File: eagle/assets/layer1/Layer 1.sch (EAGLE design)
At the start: 248 parts, among them M1C1 33nF, M1C2 680uF, M1C3 1.0uF, M1D1 RED, M1D2 BLUE, M1J1 XT30PB-F, M1Q1 AOD482, M1R1 1k, M1R10 1k, M1R11 10k, M1R12 4.7k, M1R2 1k, M1R3 3.3k, M1R4 3.3k, M1R5 1k, M1R6 1k, M1R7 1k, M1R8 10k, M1R9 10k, M2C1 33nF, M2C2 680uF, M2C3 1.0uF, M2D1 RED, M2D2 BLUE, M2J1 XT30PB-F, M2Q1 AOD482, M2R1 1k, M2R10 1k, M2R11 10k, M2R12 4.7k, M2R2 1k, M2R3 3.3k, M2R4 3.3k, M2R5 1k, M2R6 1k, M2R7 1k, M2R8 10k, M2R9 10k, M3C1 33nF, M3C2 680uF, M3C3 1.0uF, M3D1 RED, M3D2 BLUE, M3J1 XT30PB-F, M3Q1 AOD482, M3R1 1k, M3R10 1k, M3R11 10k, M3R12 4.7k, M3R2 1k, M3R3 3.3k, M3R4 3.3k, M3R5 1k, M3R6 1k, M3R7 1k, M3R8 10k, M3R9 10k, M4C1 33nF, M4C2 680uF, M4C3 1.0uF, M4D1 RED, M4D2 BLUE, M4J1 XT30PB-F, M4Q1 AOD482, M4R1 1k, M4R10 1k, M4R11 10k, M4R12 4.7k, M4R2 1k, M4R3 3.3k, M4R4 3.3k, M4R5 1k, M4R6 1k, M4R7 1k, M4R8 10k, M4R9 10k, Q1 LIGHT_SENSORALS, Q10 LIGHT_SENSORALS, Q11 LIGHT_SENSORALS, Q12 LIGHT_SENSORALS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

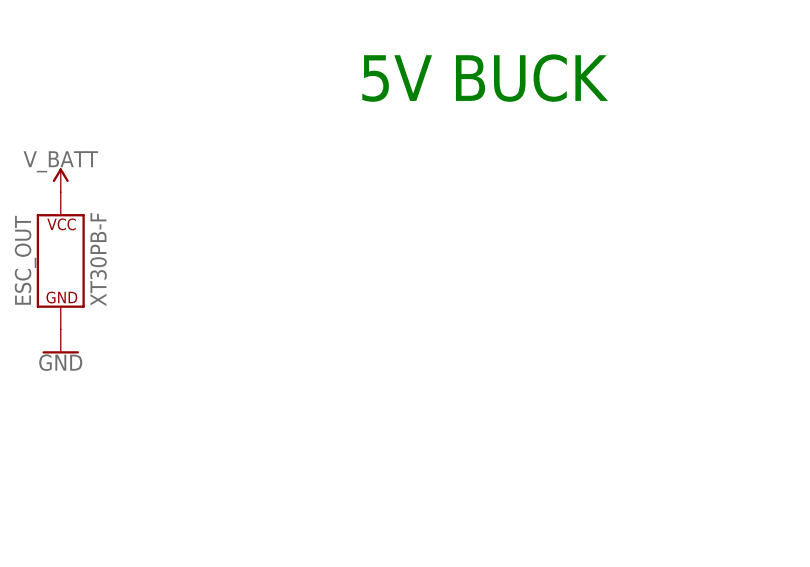
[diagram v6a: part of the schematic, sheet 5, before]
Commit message: Added GND Connector
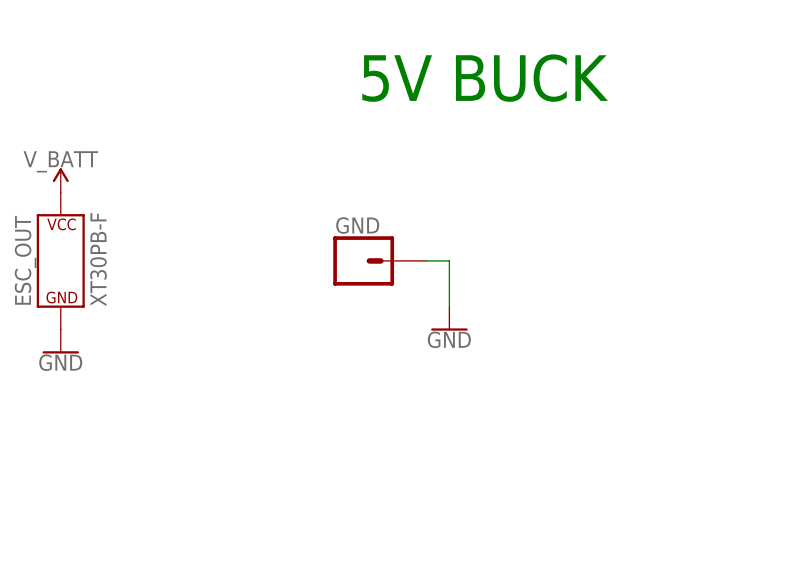
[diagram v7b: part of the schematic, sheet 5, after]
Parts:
- added GND: (no value), SparkFun-Connectors:CONN_01
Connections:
- net GND: now also GND.1
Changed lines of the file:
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@@
 <part name="R10" library="JH" library_urn="urn:adsk.eagle:library:6027132" deviceset="RESISTOR" device="0603" package3d_urn="urn:adsk.eagle:package:15441228/3" value="10k"/>
 <part name="GND40" library="SparkFun-PowerSymbols" deviceset="GND" device=""/>
+<part name="GND" library="SparkFun-Connectors" library_urn="urn:adsk.eagle:library:513" deviceset="CONN_01" device="" package3d_urn="urn:adsk.eagle:package:38028/1"/>
+<part name="GND41" library="SparkFun-PowerSymbols" deviceset="GND" device=""/>
 </parts>
 <sheets>
@@
 <attribute name="NAME" x="10.16" y="58.928" size="1.778" layer="95" font="vector"/>
 </instance>
+<instance part="GND" gate="G$1" x="43.18" y="20.32" smashed="yes">
+<attribute name="VALUE" x="40.64" y="15.494" size="1.778" layer="96" font="vector"/>
+<attribute name="NAME" x="40.64" y="23.368" size="1.778" layer="95" font="vector"/>
+</instance>
+<instance part="GND41" gate="1" x="53.34" y="12.7" smashed="yes">
+<attribute name="VALUE" x="53.34" y="12.446" size="1.778" layer="96" align="top-center"/>
+</instance>
 </instances>
 <busses>
@@
 <pinref part="GND39" gate="1" pin="GND"/>
 </segment>
+<segment>
+<pinref part="GND" gate="G$1" pin="1"/>
+<pinref part="GND41" gate="1" pin="GND"/>
+<wire x1="50.8" y1="20.32" x2="53.34" y2="20.32" width="0.1524" layer="91"/>
+<wire x1="53.34" y1="20.32" x2="53.34" y2="15.24" width="0.1524" layer="91"/>
+</segment>
 </net>

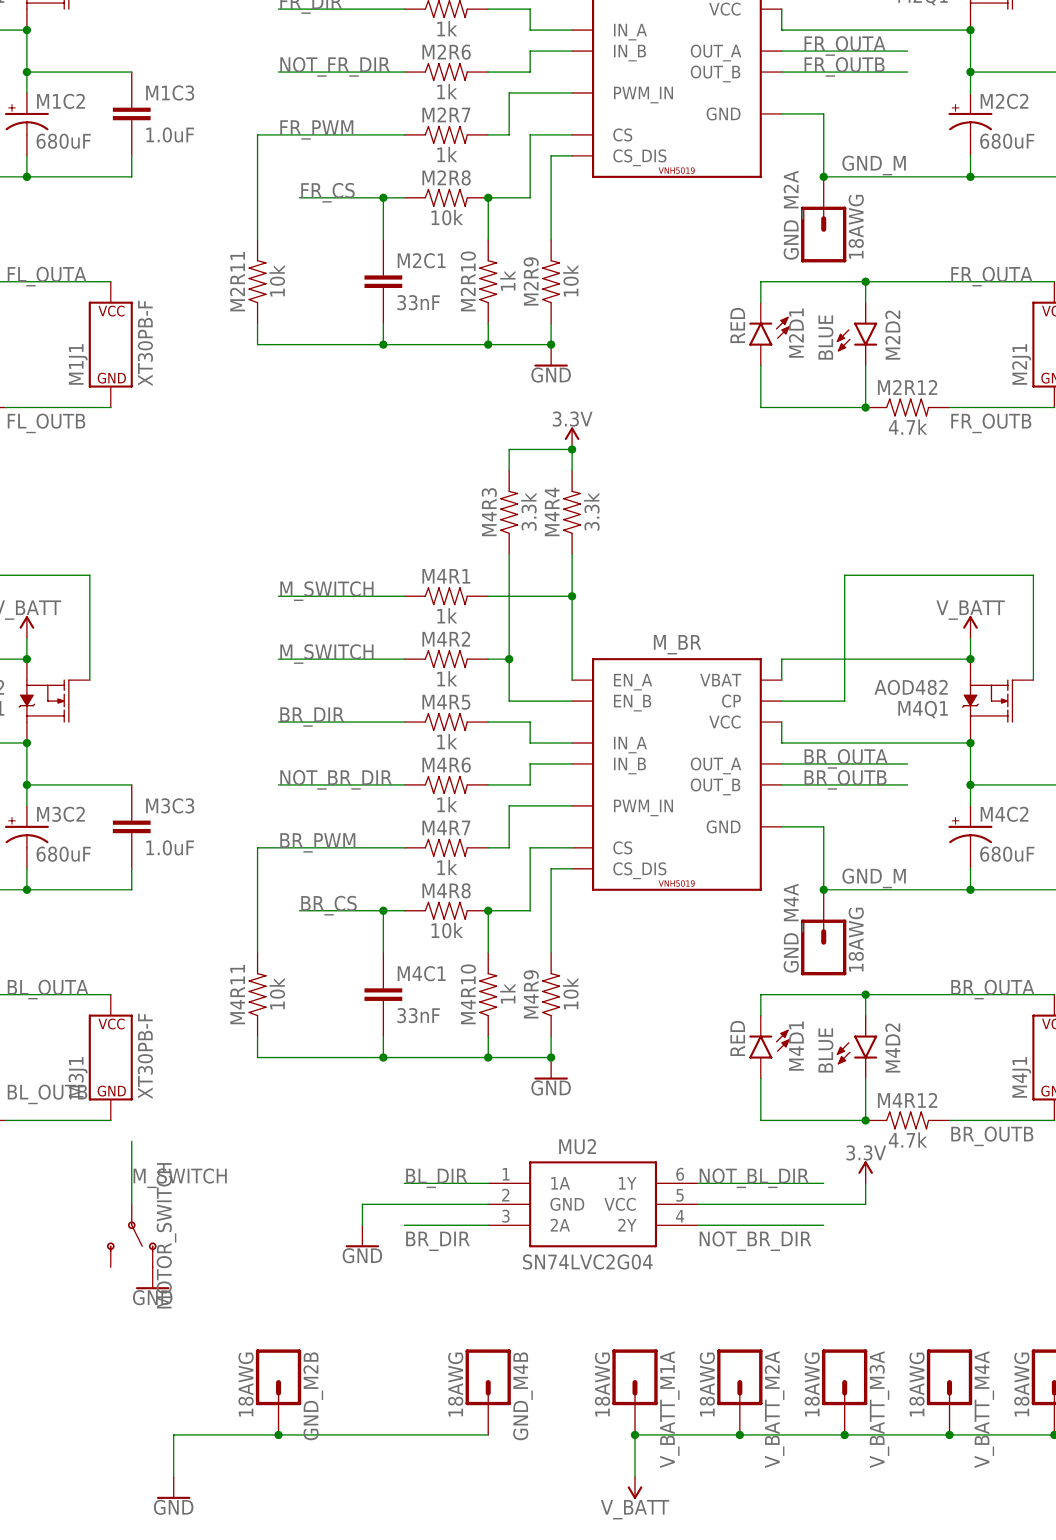
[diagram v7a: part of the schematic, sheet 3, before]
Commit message: Removed Motor Ground and Added battery mount holes
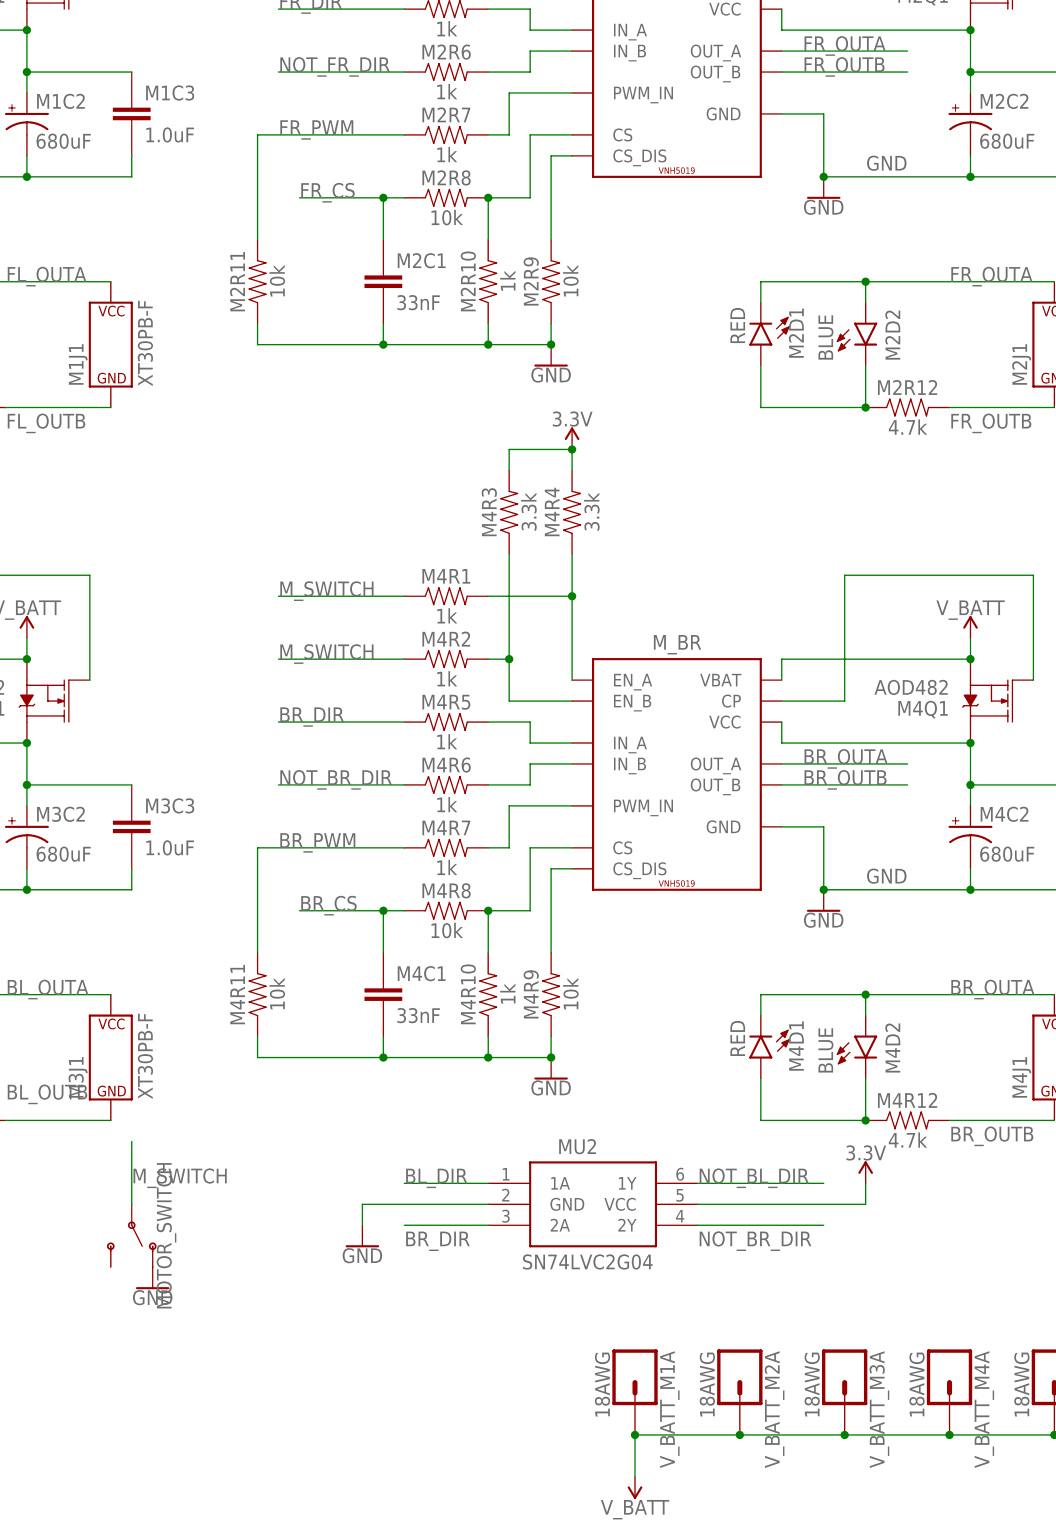
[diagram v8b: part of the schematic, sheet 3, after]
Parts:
- removed GND_M2A, GND_M2B, GND_M4A, GND_M4B: 18AWG, JH:18AWG
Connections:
- removed net GND_M: GND_M2A.1, GND_M4A.1, M2C2.-, M2C3.2, M4C2.-, M4C3.2, M_BR.GND, M_FR.GND
- net GND: now also M2C2.-, M2C3.2, M4C2.-, M4C3.2, M_BR.GND, M_FR.GND; no longer GND_M2B.1, GND_M4B.1
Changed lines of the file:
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@@
 <part name="M3J1" library="JH" library_urn="urn:adsk.eagle:library:6027132" deviceset="XT30" device="PB-F" package3d_urn="urn:adsk.eagle:package:15925142/7"/>
 <part name="M4J1" library="JH" library_urn="urn:adsk.eagle:library:6027132" deviceset="XT30" device="PB-F" package3d_urn="urn:adsk.eagle:package:15925142/7"/>
-<part name="GND_M2A" library="JH" library_urn="urn:adsk.eagle:library:6027132" deviceset="18AWG" device="" package3d_urn="urn:adsk.eagle:package:16754415/1"/>
-<part name="GND_M4A" library="JH" library_urn="urn:adsk.eagle:library:6027132" deviceset="18AWG" device="" package3d_urn="urn:adsk.eagle:package:16754415/1"/>
-<part name="GND_M2B" library="JH" library_urn="urn:adsk.eagle:library:6027132" deviceset="18AWG" device="" package3d_urn="urn:adsk.eagle:package:16754415/1"/>
-<part name="GND_M4B" library="JH" library_urn="urn:adsk.eagle:library:6027132" deviceset="18AWG" device="" package3d_urn="urn:adsk.eagle:package:16754415/1"/>
-<part name="GND6" library="SparkFun-PowerSymbols" deviceset="GND" device=""/>
 <part name="3C1" library="JH" library_urn="urn:adsk.eagle:library:6027132" deviceset="CAPACITOR" device="0603" package3d_urn="urn:adsk.eagle:package:15441226/3" value="0.1uF"/>
 <part name="3C2" library="JH" library_urn="urn:adsk.eagle:library:6027132" deviceset="CAPACITOR" device="0603" package3d_urn="urn:adsk.eagle:package:15441226/3" value="0.1uF"/>
@@
 <part name="GND" library="SparkFun-Connectors" library_urn="urn:adsk.eagle:library:513" deviceset="CONN_01" device="" package3d_urn="urn:adsk.eagle:package:38028/1"/>
 <part name="GND41" library="SparkFun-PowerSymbols" deviceset="GND" device=""/>
+<part name="GND6" library="SparkFun-PowerSymbols" deviceset="GND" device=""/>
+<part name="GND42" library="SparkFun-PowerSymbols" deviceset="GND" device=""/>
 </parts>
 <sheets>
@@
 <attribute name="VALUE" x="139.7" y="71.12" size="1.778" layer="95" font="vector" rot="R90"/>
 </instance>
-<instance part="GND_M2A" gate="G$1" x="106.68" y="175.26" smashed="yes" rot="R90">
-<attribute name="VALUE" x="111.506" y="172.72" size="1.778" layer="96" font="vector" rot="R90"/>
-<attribute name="NAME" x="103.632" y="172.72" size="1.778" layer="95" font="vector" rot="R90"/>
-</instance>
-<instance part="GND_M4A" gate="G$1" x="106.68" y="88.9" smashed="yes" rot="R90">
-<attribute name="VALUE" x="111.506" y="86.36" size="1.778" layer="96" font="vector" rot="R90"/>
-<attribute name="NAME" x="103.632" y="86.36" size="1.778" layer="95" font="vector" rot="R90"/>
-</instance>
-<instance part="GND_M2B" gate="G$1" x="40.64" y="38.1" smashed="yes" rot="R270">
-<attribute name="VALUE" x="35.814" y="40.64" size="1.778" layer="96" font="vector" rot="R270"/>
-<attribute name="NAME" x="43.688" y="40.64" size="1.778" layer="95" font="vector" rot="R270"/>
-</instance>
-<instance part="GND_M4B" gate="G$1" x="66.04" y="38.1" smashed="yes" rot="R270">
-<attribute name="VALUE" x="61.214" y="40.64" size="1.778" layer="96" font="vector" rot="R270"/>
-<attribute name="NAME" x="69.088" y="40.64" size="1.778" layer="95" font="vector" rot="R270"/>
-</instance>
-<instance part="GND6" gate="1" x="27.94" y="22.86" smashed="yes">
-<attribute name="VALUE" x="27.94" y="22.606" size="1.778" layer="96" align="top-center"/>
-</instance>
 <instance part="3C1" gate="G$1" x="-35.56" y="38.1" smashed="yes">
 <attribute name="NAME" x="-34.036" y="40.64" size="1.778" layer="95" font="vector" align="center-left"/>
@@
 <attribute name="NAME" x="175.768" y="40.64" size="1.778" layer="95" font="vector" rot="R270"/>
 </instance>
+<instance part="GND6" gate="1" x="106.68" y="93.98" smashed="yes">
+<attribute name="VALUE" x="106.68" y="93.726" size="1.778" layer="96" align="top-center"/>
+</instance>
+<instance part="GND42" gate="1" x="106.68" y="180.34" smashed="yes">
+<attribute name="VALUE" x="106.68" y="180.086" size="1.778" layer="96" align="top-center"/>
+</instance>
 </instances>
 <busses>
@@
 </segment>
 <segment>
-<pinref part="GND6" gate="1" pin="GND"/>
-<pinref part="GND_M4B" gate="G$1" pin="1"/>
-<wire x1="27.94" y1="30.48" x2="40.64" y2="30.48" width="0.1524" layer="91"/>
-<pinref part="GND_M2B" gate="G$1" pin="1"/>
-<junction x="40.64" y="30.48"/>
-<wire x1="40.64" y1="30.48" x2="66.04" y2="30.48" width="0.1524" layer="91"/>
-<wire x1="27.94" y1="30.48" x2="27.94" y2="25.4" width="0.1524" layer="91"/>
-</segment>
-<segment>
 <pinref part="3C2" gate="G$1" pin="2"/>
 <pinref part="3C1" gate="G$1" pin="2"/>
@@
 <junction x="-7.62" y="96.52"/>
 </segment>
+<segment>
+<pinref part="M_BR" gate="G$1" pin="GND"/>
+<wire x1="101.6" y1="104.14" x2="106.68" y2="104.14" width="0.1524" layer="91"/>
+<wire x1="106.68" y1="104.14" x2="106.68" y2="96.52" width="0.1524" layer="91"/>
+<pinref part="M4C2" gate="G$1" pin="-"/>
+<wire x1="124.46" y1="99.06" x2="124.46" y2="96.52" width="0.1524" layer="91"/>
+<wire x1="124.46" y1="96.52" x2="106.68" y2="96.52" width="0.1524" layer="91"/>
+<pinref part="M4C3" gate="G$1" pin="2"/>
+<wire x1="137.16" y1="99.06" x2="137.16" y2="96.52" width="0.1524" layer="91"/>
+<wire x1="137.16" y1="96.52" x2="124.46" y2="96.52" width="0.1524" layer="91"/>
+<junction x="124.46" y="96.52"/>
+<label x="116.84" y="99.06" size="1.778" layer="95" rot="R180"/>
+<pinref part="GND6" gate="1" pin="GND"/>
+<junction x="106.68" y="96.52"/>
+</segment>
+<segment>
+<pinref part="M_FR" gate="G$1" pin="GND"/>
+<wire x1="101.6" y1="190.5" x2="106.68" y2="190.5" width="0.1524" layer="91"/>
+<wire x1="106.68" y1="190.5" x2="106.68" y2="182.88" width="0.1524" layer="91"/>
+<pinref part="M2C2" gate="G$1" pin="-"/>
+<wire x1="124.46" y1="185.42" x2="124.46" y2="182.88" width="0.1524" layer="91"/>
+<wire x1="124.46" y1="182.88" x2="106.68" y2="182.88" width="0.1524" layer="91"/>
+<pinref part="M2C3" gate="G$1" pin="2"/>
+<wire x1="137.16" y1="185.42" x2="137.16" y2="182.88" width="0.1524" layer="91"/>
+<wire x1="137.16" y1="182.88" x2="124.46" y2="182.88" width="0.1524" layer="91"/>
+<junction x="124.46" y="182.88"/>
+<label x="116.84" y="185.42" size="1.778" layer="95" rot="R180"/>
+<pinref part="GND42" gate="1" pin="GND"/>
+<junction x="106.68" y="182.88"/>
+</segment>
 </net>
 <net name="N$15" class="0">
@@
 </segment>
 </net>
-<net name="GND_M" class="0">
-<segment>
-<pinref part="M_FR" gate="G$1" pin="GND"/>
-<wire x1="101.6" y1="190.5" x2="106.68" y2="190.5" width="0.1524" layer="91"/>
-<wire x1="106.68" y1="190.5" x2="106.68" y2="182.88" width="0.1524" layer="91"/>
-<pinref part="M2C2" gate="G$1" pin="-"/>
-<wire x1="124.46" y1="185.42" x2="124.46" y2="182.88" width="0.1524" layer="91"/>
-<wire x1="124.46" y1="182.88" x2="106.68" y2="182.88" width="0.1524" layer="91"/>
-<pinref part="M2C3" gate="G$1" pin="2"/>
-<wire x1="137.16" y1="185.42" x2="137.16" y2="182.88" width="0.1524" layer="91"/>
-<wire x1="137.16" y1="182.88" x2="124.46" y2="182.88" width="0.1524" layer="91"/>
-<junction x="124.46" y="182.88"/>
-<pinref part="GND_M2A" gate="G$1" pin="1"/>
-<junction x="106.68" y="182.88"/>
-<label x="116.84" y="185.42" size="1.778" layer="95" rot="R180"/>
-</segment>
-<segment>
-<pinref part="M_BR" gate="G$1" pin="GND"/>
-<wire x1="101.6" y1="104.14" x2="106.68" y2="104.14" width="0.1524" layer="91"/>
-<wire x1="106.68" y1="104.14" x2="106.68" y2="96.52" width="0.1524" layer="91"/>
-<pinref part="M4C2" gate="G$1" pin="-"/>
-<wire x1="124.46" y1="99.06" x2="124.46" y2="96.52" width="0.1524" layer="91"/>
-<wire x1="124.46" y1="96.52" x2="106.68" y2="96.52" width="0.1524" layer="91"/>
-<pinref part="M4C3" gate="G$1" pin="2"/>
-<wire x1="137.16" y1="99.06" x2="137.16" y2="96.52" width="0.1524" layer="91"/>
-<wire x1="137.16" y1="96.52" x2="124.46" y2="96.52" width="0.1524" layer="91"/>
-<junction x="124.46" y="96.52"/>
-<pinref part="GND_M4A" gate="G$1" pin="1"/>
-<junction x="106.68" y="96.52"/>
-<label x="116.84" y="99.06" size="1.778" layer="95" rot="R180"/>
-</segment>
-</net>
